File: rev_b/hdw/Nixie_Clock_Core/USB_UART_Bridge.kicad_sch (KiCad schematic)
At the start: 34 parts, among them J1301 USB_B_Mini, U1301 TLV6700, U1302 FT234XD, U1304 TXB0102DCU, U1305 TPD3S014DBVR

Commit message: lots of rev B control board schematic progress
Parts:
- removed C1310, C1312: 0.1uF, Capacitors_SMD:C_0603, symbol Custom_Library:C_Custom
- removed R? (x2): 10, Resistors_SMD:R_0603, symbol Custom_Library:R_Custom
- removed R?: 0.02, Resistors_SMD:R_0612, symbol Custom_Library:R_Custom
- removed U1304: TXB0102DCU, Package_SO:VSSOP-8_2.4x2.1mm_P0.5mm, symbol Logic_LevelTranslator:TXB0102DCU
- added C?: 0.1uF, Capacitors_SMD:C_0402, symbol Custom_Library:C_Custom
- added D?: Green, LEDs:LED_0402, symbol Device:LED
- added R?: 1k, Resistors_SMD:R_0402, symbol Custom_Library:R_Custom
- added U?: 74LVC1G97, Package_TO_SOT_SMD:SOT-363_SC-70-6, symbol Custom Library:74LVC1G97_Power_NOT
- added U?: ISO7321C, Package_SO:SOIC-8_3.9x4.9mm_P1.27mm, symbol Isolator:ISO7321C
- renumbered C1307 to C?, C1309 to C?, C1311 to C?, C1302 to C?, C1306 to C?, C1301 to C?, D1301 to D?, DOC1301 to DOC?, J1301 to J?, L1301 to L?, L1302 to L?, R1314 to R?, R1312 to R?, R1302 to R?, R1311 to R?, R1305 to R?, R1315 to R?, R1304 to R?, R1301 to R?, R1306 to R?, R1303 to R?, R1308 to R?, U1302 to U?, U1301 to U?, U1305 to U?
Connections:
- net +3.3V: now also U?.1 (VCC1); no longer C?.1, R?.1, U?.5 (Vs)
- net +3.3V_USB: now also C?.1, R?.1, U?.5 (Vs), C?.1, R?.1, U?.1 (VCC), U?.5 (VCC), U?.8 (VCC2)
- net +5V_USB: now also U?.4 (OUT)
- net GND: now also U?.4 (GND1); no longer C?.2, C?.2, C?.2, C?.2, C?.2, C?.2, C?.2, C?.2, J?.5 (GND), L?.1, R?.2, U?.13 (GND), U?.2 (GND), U?.2 (GND), U?.5 (GND)
- net POS5_USB_PGOOD: now also U?.6
- net USB_UART_RX: now also U?.2 (OUTA)
- net USB_UART_TX: now also U?.3 (INB)
- net USB_UART_RX_BUF renamed USB_UART_RX_ISO
- net USB_UART_RX_ISO: now also U?.7 (INA)
- net USB_UART_TX_BUF renamed USB_UART_TX_ISO
- net USB_UART_TX_ISO: now also U?.6 (OUTB)
- new net: D?.1 (K), U?.4
- new net: D?.2 (A), R?.2
- new net GND_USB: C?.2, C?.2, C?.2, C?.2, C?.2, C?.2, C?.2, C?.2, C?.2, J?.5 (GND), L?.1, R?.2, U?.13 (GND), U?.2 (GND), U?.2 (GND), U?.2 (GND), U?.3 (GND), U?.5 (GND), U?.5 (GND2)
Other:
- moved on the sheet: C?, D?, J?, L?, R?, TP?, U?

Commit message: more rev b sch progress
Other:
- moved on the sheet: C?, D?, J?, L?, R?, TP?, U?

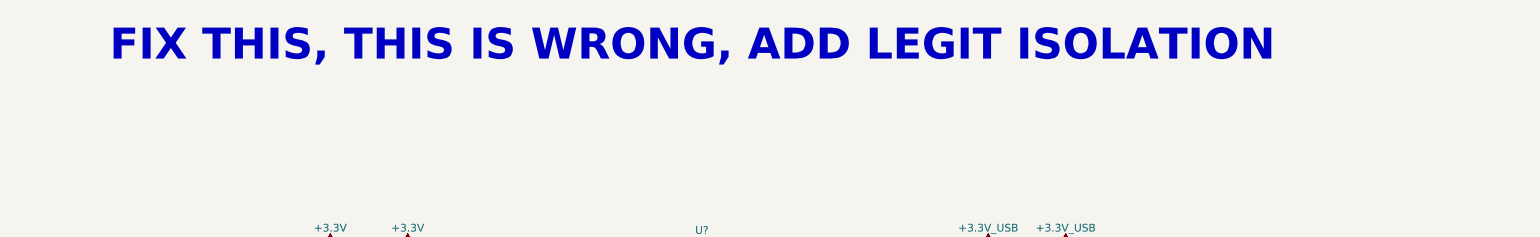
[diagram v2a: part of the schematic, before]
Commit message: more schematic progress, assigning signals to MCU"
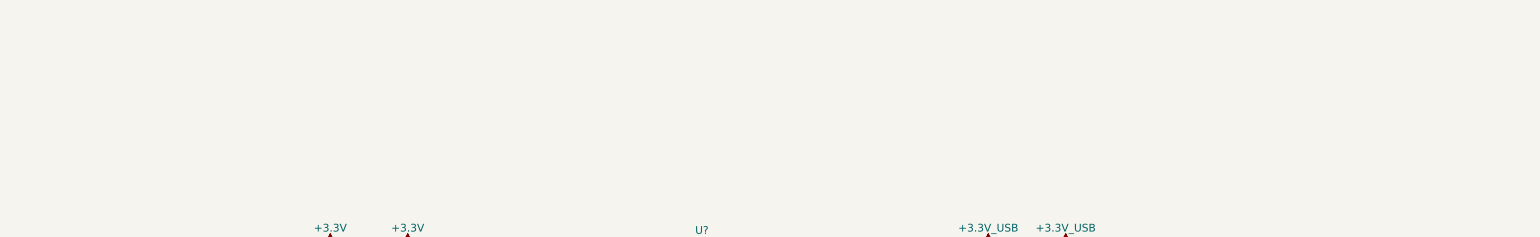
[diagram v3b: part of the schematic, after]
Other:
- note removed: "FIX THIS, THIS IS WRONG, ADD LEGIT ISOLATION"
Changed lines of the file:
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@@
     (stroke (width 0) (type default))
-  )
-  (text "FIX THIS, THIS IS WRONG, ADD LEGIT ISOLATION" (at 37.465 -6.35 0)
-    (effects (font (face "Courier New") (size 5.08 5.08) (thickness 0.254) bold (color 255 37 56 1)) (justify left bottom))
   )
   (label "BRIDGE_USB-" (at 97.79 96.52 0) (fields_autoplaced)

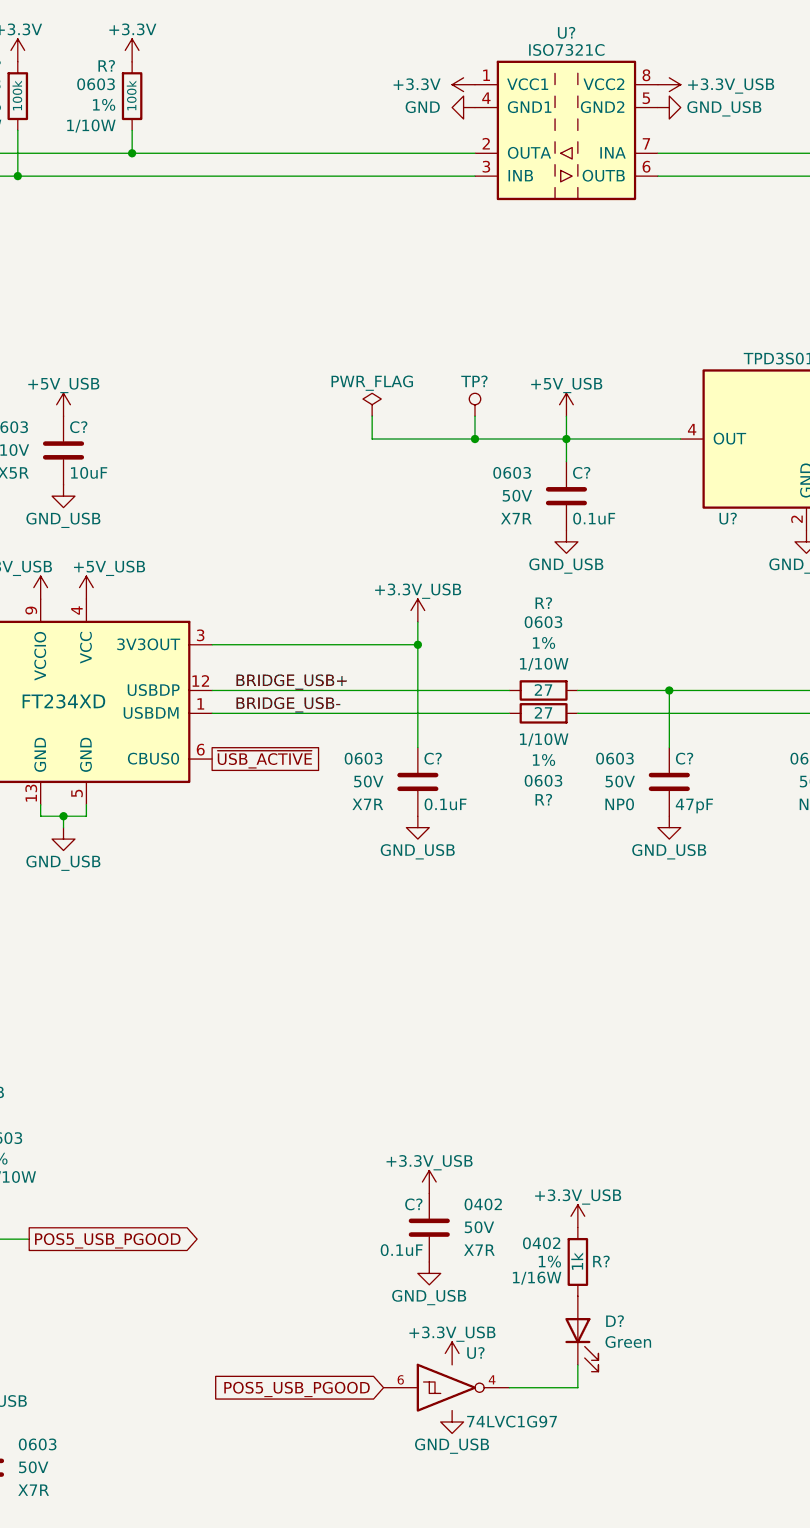
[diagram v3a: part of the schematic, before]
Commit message: updated footprints, ran some DRC
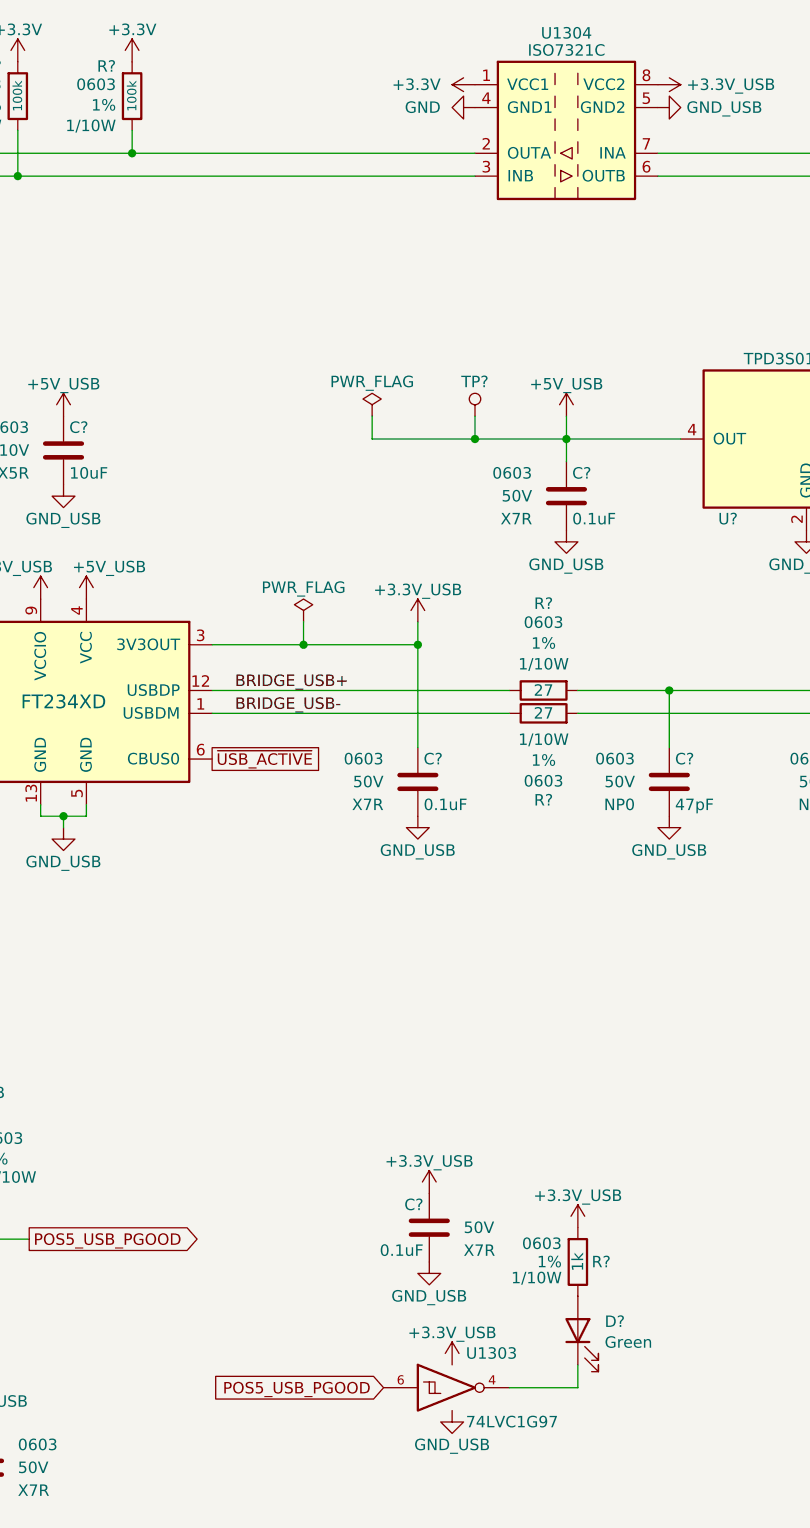
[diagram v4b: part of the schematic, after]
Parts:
- C? (x5): Digi-Key PN 399-7845-1-ND -> (none)
- C?: footprint Capacitors_SMD:C_0402 -> Capacitors_SMD:C_0603; Digi-Key PN 490-10698-1-ND -> (none); display_footprint 0402 -> (none)
- C? (x2): Digi-Key PN 399-7918-1-ND -> (none)
- C?: Digi-Key PN 490-10474-1-ND -> (none)
- D?: footprint LEDs:LED_0402 -> LEDs:LED_0603; Digi-Key PN 1497-1219-1-ND -> 754-1121-1-ND
- L? (x2): Digi-Key PN 732-1593-1-ND -> (none)
- R? (x4): Digi-Key PN RMCF0603FT100KCT-ND -> (none)
- R? (x2): Digi-Key PN 311-27.0HRCT-ND -> (none)
- R?: Digi-Key PN 311-487KHRCT-ND -> (none)
- R?: Digi-Key PN YAG2321CT-ND -> (none)
- R?: Digi-Key PN RMCF0603FT40K2CT-ND -> (none)
- R?: Digi-Key PN 311-1.00KHRCT-ND -> (none)
- R?: Digi-Key PN RMCF0603FT6K04CT-ND -> (none)
- R?: footprint Resistors_SMD:R_0402 -> Resistors_SMD:R_0603; Digi-Key PN RMCF0402FT1K00CT-ND -> (none); Wattage 1/16W -> 1/10W; display_footprint 0402 -> 0603
- gave numbers to parts that had none: 2

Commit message: hid all passive refdes on core PCB
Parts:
- C? (x5): Digi-Key PN (none) -> 1276-1935-1-ND
- C?: Digi-Key PN (none) -> 1276-1935-1-ND; display_footprint (none) -> 0603
- C? (x2): Digi-Key PN (none) -> 13-CC0603JPNPO9BN470CT-ND
- C?: Digi-Key PN (none) -> 1276-1871-1-ND
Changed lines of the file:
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@@
       (effects (font (size 1.27 1.27)) (justify right))
     )
-    (property "Digi-Key PN" "" (at 128.905 91.44 0)
+    (property "Digi-Key PN" "1276-1935-1-ND" (at 128.905 91.44 0)
       (effects (font (size 1.524 1.524)) hide)
     )
@@
       (effects (font (size 1.27 1.27)) hide)
     )
-    (property "Digi-Key PN" "" (at 108.585 140.97 0)
+    (property "Digi-Key PN" "1276-1935-1-ND" (at 108.585 140.97 0)
       (effects (font (size 1.524 1.524)) hide)
     )
-    (property "display_footprint" "" (at 123.19 151.13 0)
+    (property "display_footprint" "0603" (at 123.19 151.13 0)
       (effects (font (size 1.27 1.27)) (justify right))
     )
@@
       (effects (font (size 1.27 1.27)) hide)
     )
-    (property "Digi-Key PN" "" (at 59.055 167.64 0)
+    (property "Digi-Key PN" "1276-1935-1-ND" (at 59.055 167.64 0)
       (effects (font (size 1.524 1.524)) hide)
     )
@@
       (effects (font (size 1.27 1.27)) (justify right))
     )
-    (property "Digi-Key PN" "" (at 146.05 104.14 0)
+    (property "Digi-Key PN" "13-CC0603JPNPO9BN470CT-ND" (at 146.05 104.14 0)
       (effects (font (size 1.27 1.27)) hide)
     )
@@
       (effects (font (size 1.27 1.27)) (justify right))
     )
-    (property "Digi-Key PN" "" (at 167.64 104.14 0)
+    (property "Digi-Key PN" "13-CC0603JPNPO9BN470CT-ND" (at 167.64 104.14 0)
       (effects (font (size 1.27 1.27)) hide)
     )
@@
       (effects (font (size 1.27 1.27)) (justify right))
     )
-    (property "Digi-Key PN" "" (at 78.74 67.31 0)
+    (property "Digi-Key PN" "1276-1871-1-ND" (at 78.74 67.31 0)
       (effects (font (size 1.27 1.27)) hide)
     )
@@
       (effects (font (size 1.27 1.27)) (justify right))
     )
-    (property "Digi-Key PN" "" (at 73.025 54.61 0)
+    (property "Digi-Key PN" "1276-1935-1-ND" (at 73.025 54.61 0)
       (effects (font (size 1.524 1.524)) hide)
     )
@@
       (effects (font (size 1.27 1.27)) (justify right))
     )
-    (property "Digi-Key PN" "" (at 145.415 59.69 0)
+    (property "Digi-Key PN" "1276-1935-1-ND" (at 145.415 59.69 0)
       (effects (font (size 1.524 1.524)) hide)
     )
@@
       (effects (font (size 1.27 1.27)) (justify right))
     )
-    (property "Digi-Key PN" "" (at 55.245 54.61 0)
+    (property "Digi-Key PN" "1276-1935-1-ND" (at 55.245 54.61 0)
       (effects (font (size 1.524 1.524)) hide)
     )

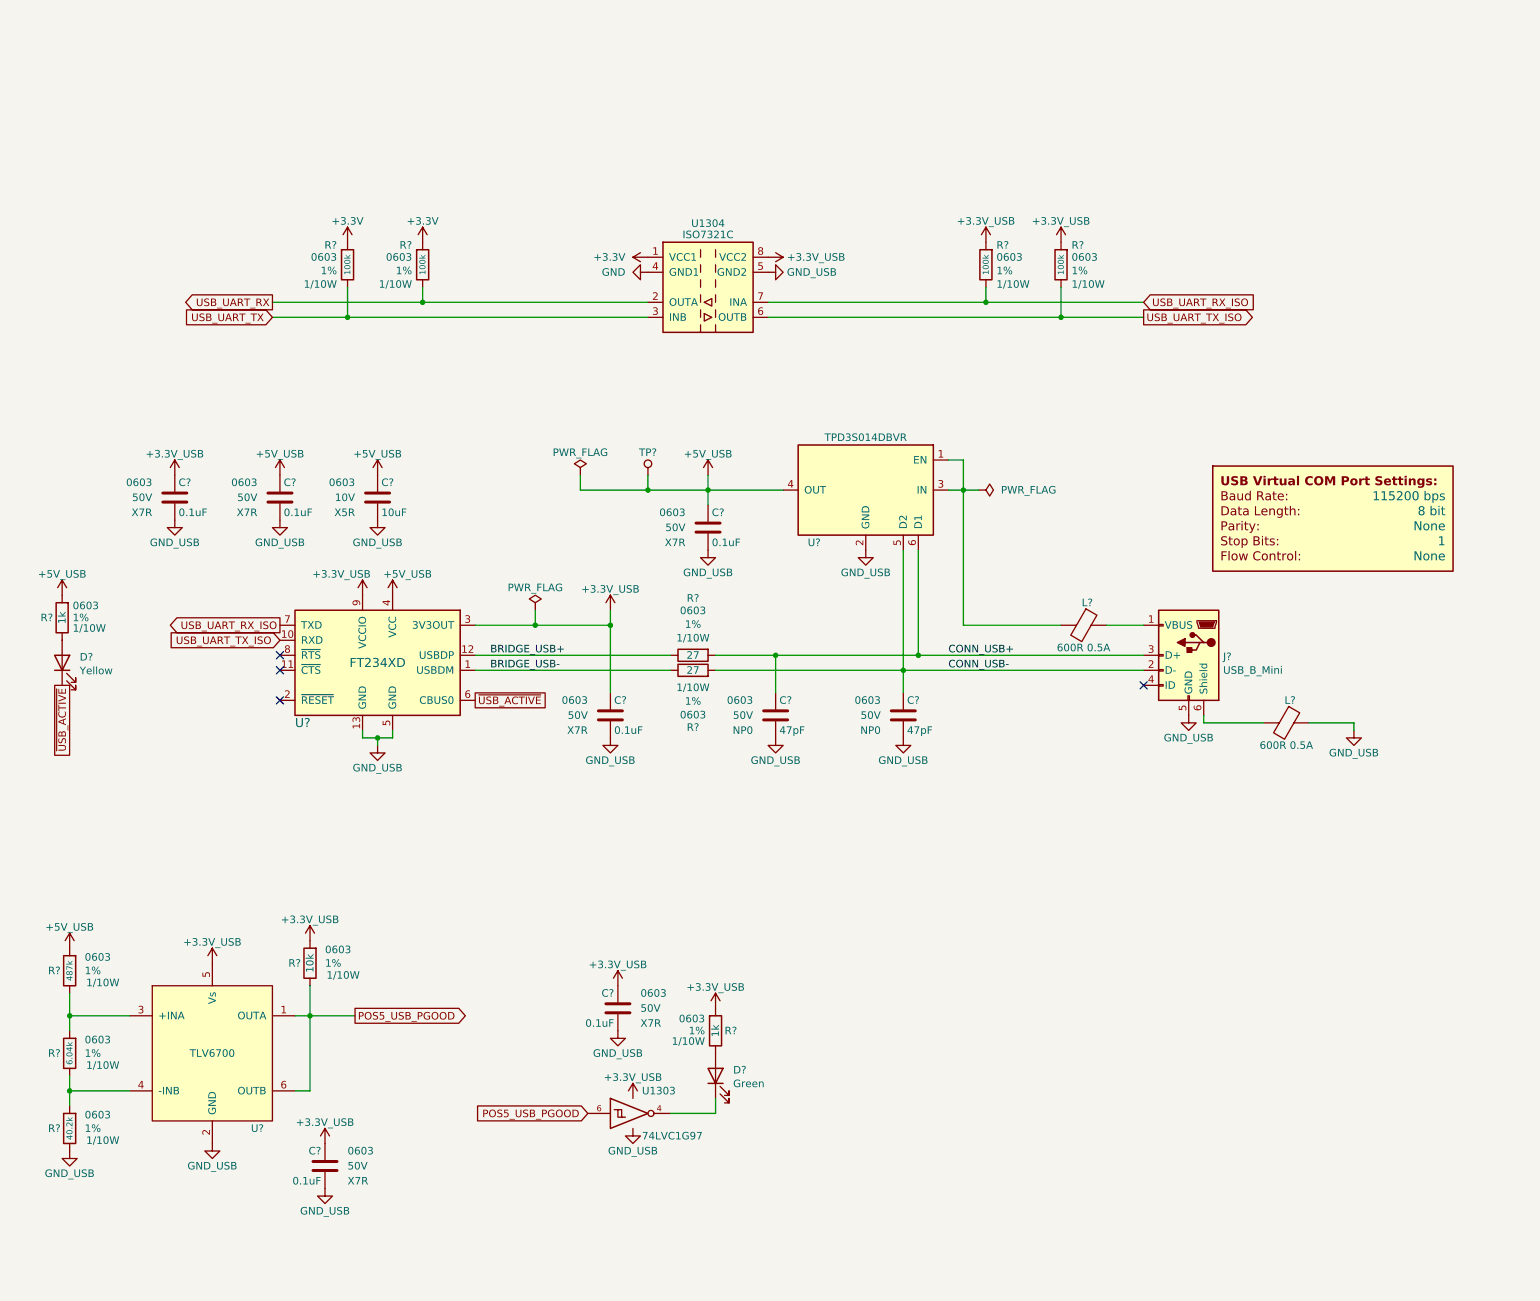
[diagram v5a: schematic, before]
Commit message: arranged USB components on PCB, added USB isolator Bypass
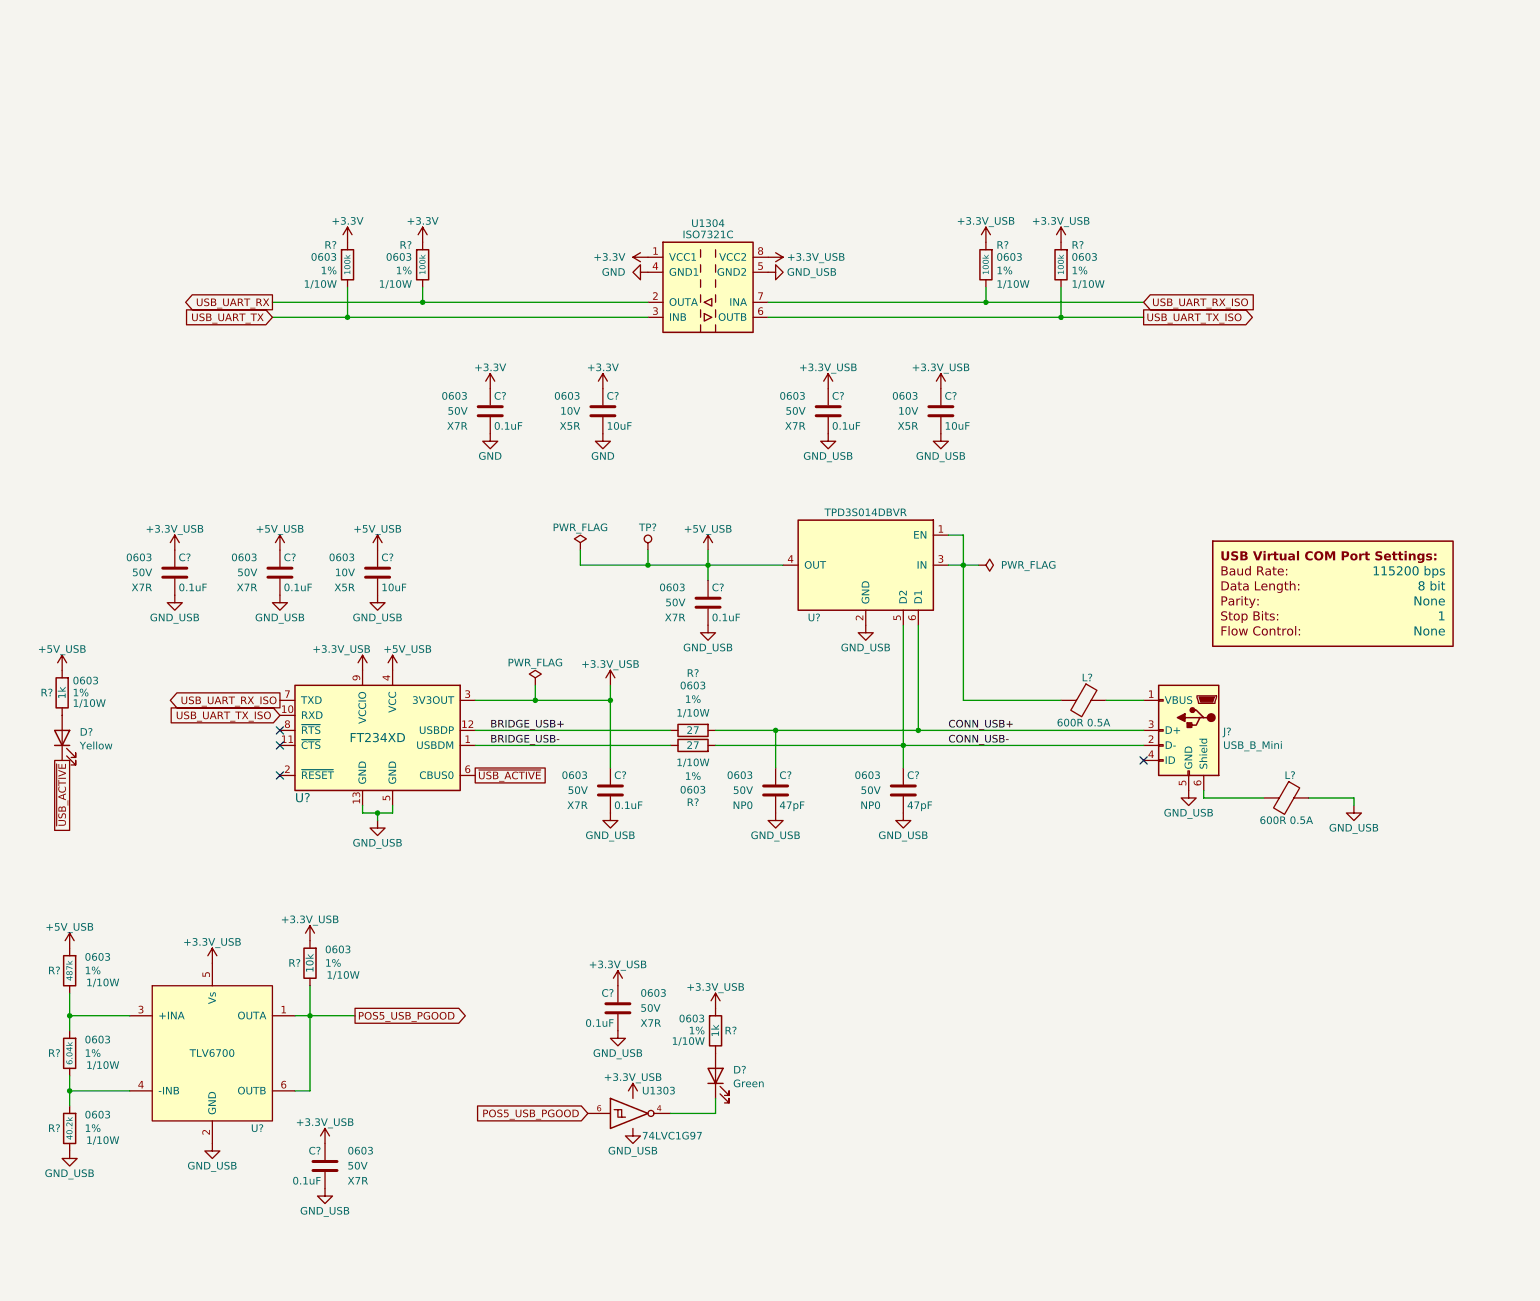
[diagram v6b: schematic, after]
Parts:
- added C? (x2): 10uF, Capacitors_SMD:C_0603, symbol Custom_Library:C_Custom
- added C? (x2): 0.1uF, Capacitors_SMD:C_0603, symbol Custom_Library:C_Custom
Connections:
- net +3.3V: now also C?.1, C?.1
- net +3.3V_USB: now also C?.1, C?.1
- net GND: now also C?.2, C?.2
- net GND_USB: now also C?.2, C?.2
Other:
- moved on the sheet: C?, D?, J?, L?, R?, TP?, U?
